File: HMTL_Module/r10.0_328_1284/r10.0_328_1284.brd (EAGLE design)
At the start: 79.7 x 61 mm, 39 parts, among them J2 AVR_SPI_PRG_6PTH, Y1 20MHz

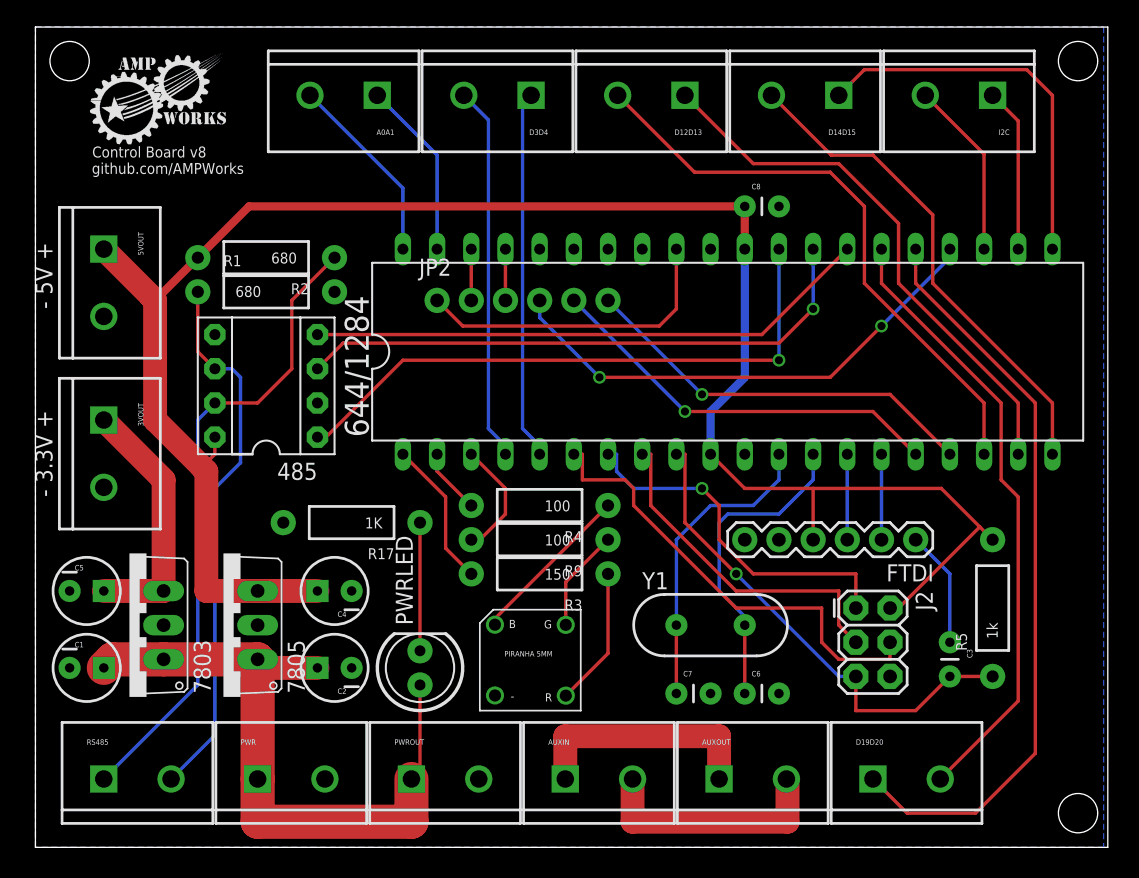
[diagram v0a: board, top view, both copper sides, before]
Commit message: Added correct 328 plus 1284 layout based on most recent 1284 layout
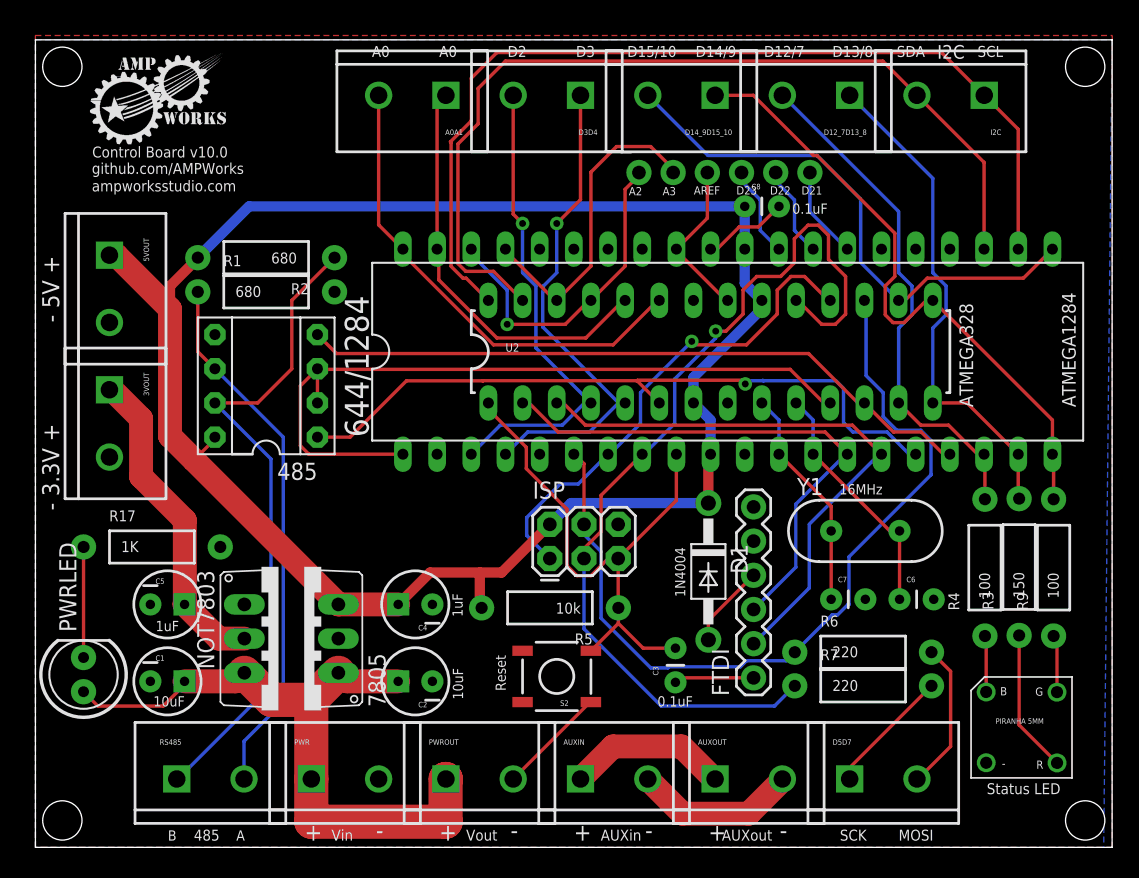
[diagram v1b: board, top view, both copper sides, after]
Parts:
- removed 7803: 7805TV, linear:TO220V
- removed D12D13, D14D15, D19D20: M025MM, SparkFun-Connectors:SCREWTERMINAL-5MM-2
- removed FRAME1: FRAME-LETTER, SparkFun-Aesthetics:CREATIVE_COMMONS
- removed J2: AVR_SPI_PRG_6PTH, SparkFun-Connectors:2X3
- removed JP2: (no value), SparkFun-Connectors:1X06_NO_SILK
- added D1: 1N4004, adafruit:DO41-10
- added D12_7D13_8, D14_9D15_10, D5D7: M025MM, SparkFun-Connectors:SCREWTERMINAL-5MM-2
- added ISP: AVR_SPI_PRG_6PTH, SparkFun-Connectors:2X3
- added NOT7803: 7805TV, linear:TO220V
- added R6, R7: 220, SparkFun-Passives:AXIAL-0.4
- added S2: Reset, SparkFun:TACTILE_SWITCH_SMD
- added U2: ATMEGA328P_PDIP, SparkFun-DigitalIC:DIL28-3
- added _: (no value), SparkFun-Connectors:1X06_NO_SILK
- R5: value 1k -> 10k
- Y1: value 20MHz -> 16MHz
- moved R9 38.2 mm to (75.7, 20.8), turned to 90 degrees
- moved STATUS 36.8 mm to (73.3, 8.97)
- moved R3 35.6 mm to (73.1, 20.8), turned to 90 degrees
- moved R4 33.4 mm to (70.5, 20.8), turned to 90 degrees
- moved R5 32.9 mm to (38.2, 17.8), turned to 180 degrees
- moved PWRLED 25.0 mm to (3.58, 12.8)
- moved C3 20.6 mm to (47.6, 12.3), turned to 90 degrees
- moved FTDI 15.8 mm to (53.4, 12.6), turned to 90 degrees
- moved R17 14.9 mm to (8.65, 22.3), turned to 0 degrees
- moved C6 13.5 mm to (64.2, 18.4)
- moved C7 13.5 mm to (59.1, 18.4)
- moved Y1 13.5 mm to (61.7, 23.5)
- moved 7805 6.08 mm to (20.0, 15.5)
- moved C1 6.08 mm to (9.81, 12.3)
- moved C2 6.08 mm to (28.2, 12.3)
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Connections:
- removed net CTS: FTDI.CTS
- removed net D10: 644/1284.16, JP2.5
- removed net D11: 644/1284.17, JP2.6
- removed net D12: 644/1284.18, D12D13.2
- removed net D13: 644/1284.19, D12D13.1
- removed net D14: 644/1284.20, D14D15.2
- removed net D15: 644/1284.21, D14D15.1
- removed net LED1: 644/1284.1, R3.P$2
- removed net LED2: 644/1284.2, R4.P$2
- removed net LED3: 644/1284.3, R9.P$2
- new net D1: 644/1284.2
- new net D12D7: 644/1284.18, D12_7D13_8.2, R4.P$2, U2.13
- new net D13D8: 644/1284.19, D12_7D13_8.1, R3.P$2, U2.14
- new net D14D9: 644/1284.20, D14_9D15_10.1, R9.P$2, U2.15
- new net D15D10: 644/1284.21, D14_9D15_10.2, U2.16
- new net D2: 644/1284.3, D3D4.2, U2.4
- new net D21: 644/1284.27, _.6
- new net D22: 644/1284.28, _.5
- new net D23: 644/1284.29, _.4
- new net N$4: D5D7.2, R6.P$2
- new net N$8: D5D7.1, R7.P$2
- new net N$9: D1.A, FTDI.VCC
- net 3VVCC: now also NOT7803.2; no longer 7803.3
- net A0: now also U2.23
- net A1: now also U2.24
- net A2: now also U2.25, _.1; no longer JP2.2
- net A3: now also U2.26, _.2; no longer JP2.3
- net AREF: now also U2.21, _.3; no longer JP2.1
- net CLK1: now also U2.9
- net CLK2: now also U2.10
- net D18: no longer JP2.4
- net D19: no longer D19D20.1
- net D20: no longer D19D20.2
- net D3: now also D3D4.1, U2.5; no longer D3D4.2
- net D4: no longer D3D4.1
- net GND: now also FTDI.CTS, ISP.6, NOT7803.1, S2.1, U2.22, U2.8; no longer 485.2, 7803.2, J2.6
- net MISO: now also ISP.1, U2.18; no longer J2.1
- net MOSI: now also ISP.4, R6.P$1, U2.17; no longer J2.4
- net PWR+: now also NOT7803.3; no longer 7803.1
- net RESET: now also ISP.5, S2.3, U2.1; no longer J2.5
- net RS485DE: now also 485.2, 644/1284.1, U2.11; no longer 644/1284.28
- net RS485DI: now also 644/1284.17, U2.12; no longer 644/1284.27
- net RS485RO: now also 644/1284.16, U2.6; no longer 644/1284.29
- net RX: now also U2.2
- net SCK: now also ISP.3, R7.P$1, U2.19; no longer J2.3
- net SCL: now also U2.28
- net SDA: now also U2.27
- net TX: now also U2.3
- net VCC: now also D1.C, ISP.2, U2.20, U2.7; no longer FTDI.VCC, J2.2
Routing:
- net SCL: track 12.2 -> 71.2 mm
- net D19: track 56.1 -> 0.00 mm
- net SDA: track 13.2 -> 67.6 mm
- net D14D9: track 0.00 -> 46.9 mm
- net D20: track 46.0 -> 0.00 mm
- net SCK: track 25.4 -> 70.0 mm, vias 0 -> 1
- net D12: track 43.9 -> 0.00 mm
- net D15D10: track 0.00 -> 40.7 mm
- net D13: track 40.6 -> 0.00 mm
- net D12D7: track 0.00 -> 38.6 mm
- net D18: track 37.9 -> 0.00 mm, vias 2 -> 0
- net D13D8: track 0.00 -> 37.5 mm
- net TX: track 6.35 -> 43.8 mm
- net D14: track 37.1 -> 0.00 mm
- net D2: track 0.00 -> 35.7 mm, vias 0 -> 1
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- added copper zone on layer 1, net GND
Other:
- board size 79.7 x 61 mm -> 80 x 60 mm
- board text added: "+"
- board text added: "-"
- board text added: "0.1uF"
- board text added: "10uF"
- board text added: "16MHz"
- board text added: "1N4004"
- board text added: "1uF"
- board text added: "485"
- board text added: "A"
- board text added: "A0"
- board text added: "ATMEGA1284"
- board text added: "ATMEGA328"
- board text added: "AUXin"
- board text added: "AUXout"
- board text added: "B"
- board text added: "Control Board v10.0"
- board text added: "D12/7"
- board text added: "D13/8"
- board text added: "D14/9"
- board text added: "D15/10"
- board text added: "D2"
- board text added: "D21"
- board text added: "D22"
- board text added: "D23"
- board text added: "D3"
- board text added: "I2C"
- board text added: "MOSI"
- board text added: "Reset"
- board text added: "SCK"
- board text added: "SCL"
- board text added: "SDA"
- board text added: "Status LED"
- board text added: "Vin"
- board text added: "Vout"
- board text added: "ampworksstudio.com"
- board text removed: "Control Board v8"
- board text removed: "D10"
- board text removed: "D11"
- board text removed: "D18"
